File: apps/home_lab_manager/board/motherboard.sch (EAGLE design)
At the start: 18 parts, among them X1 22-23-2021

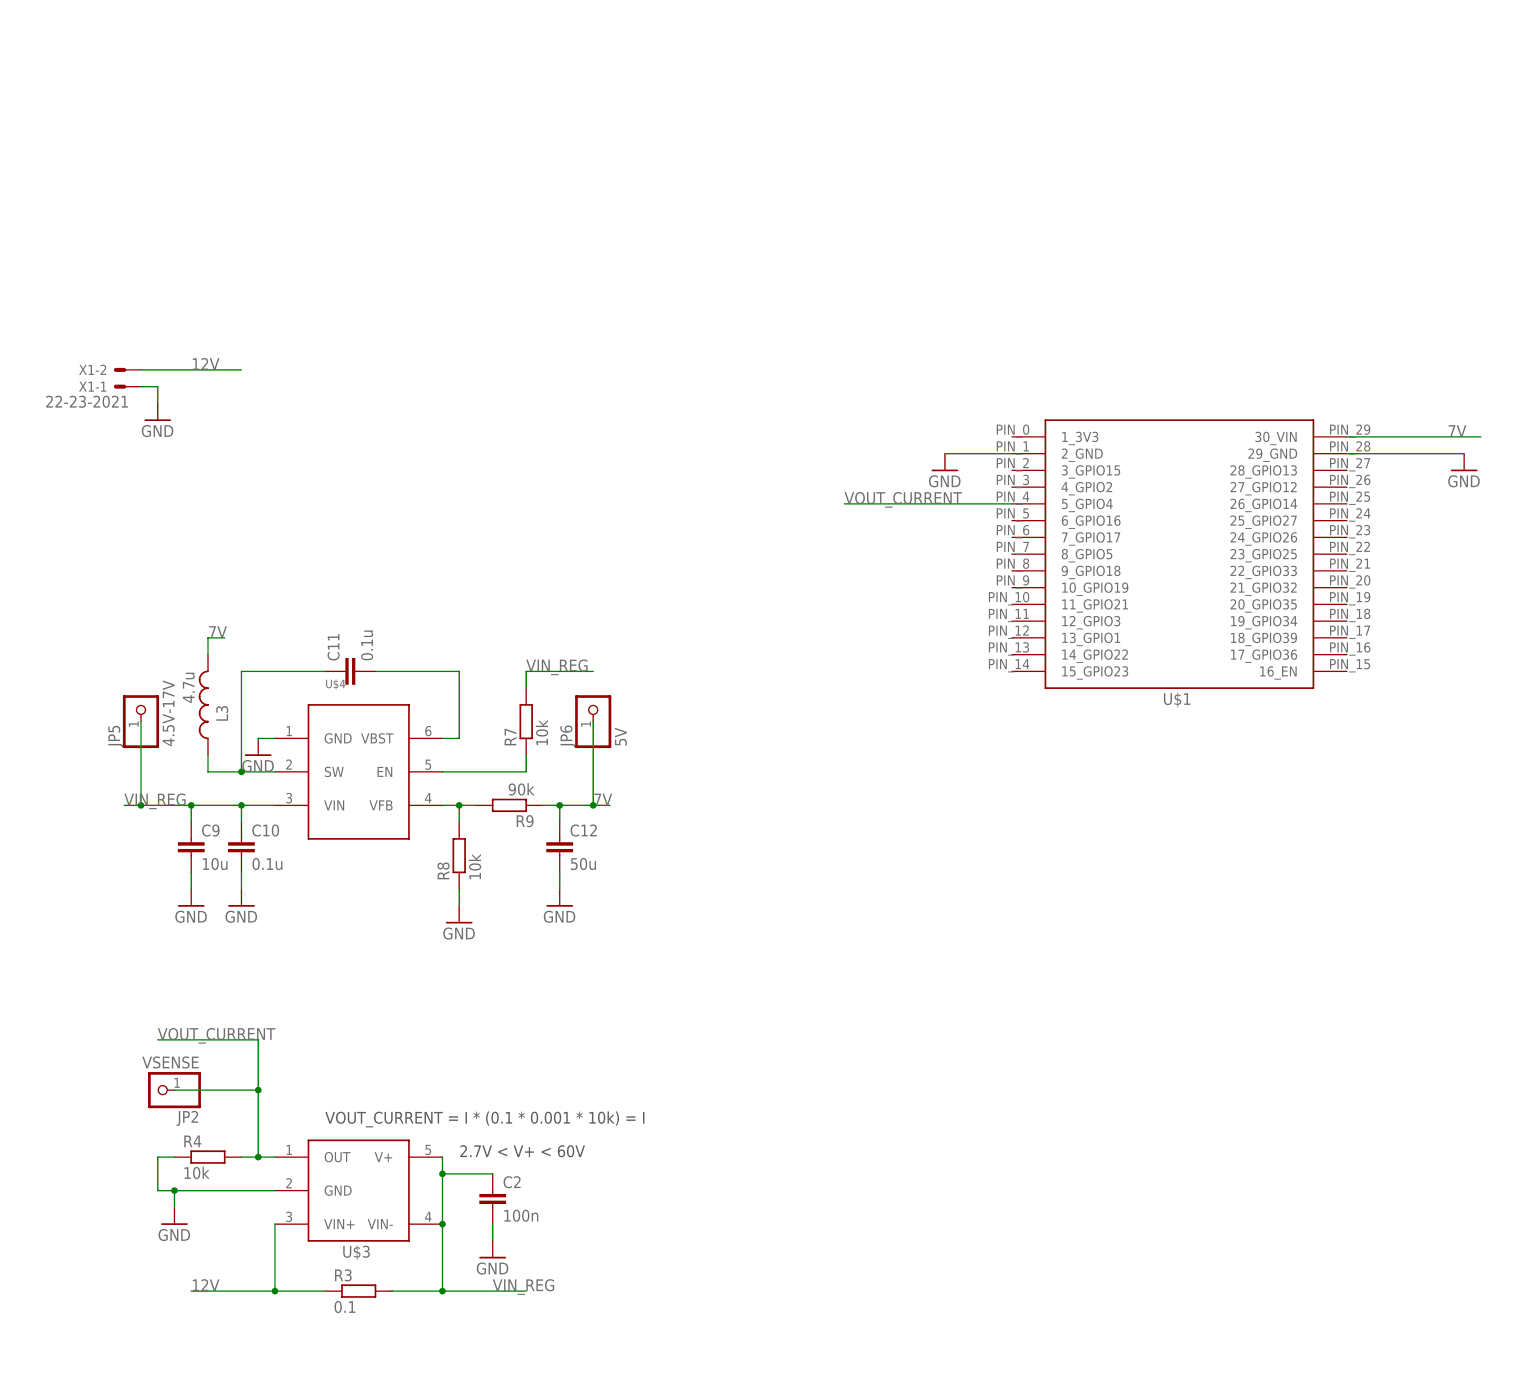
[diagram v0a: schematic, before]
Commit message: Adding mq-2 gaz sensor (wip)
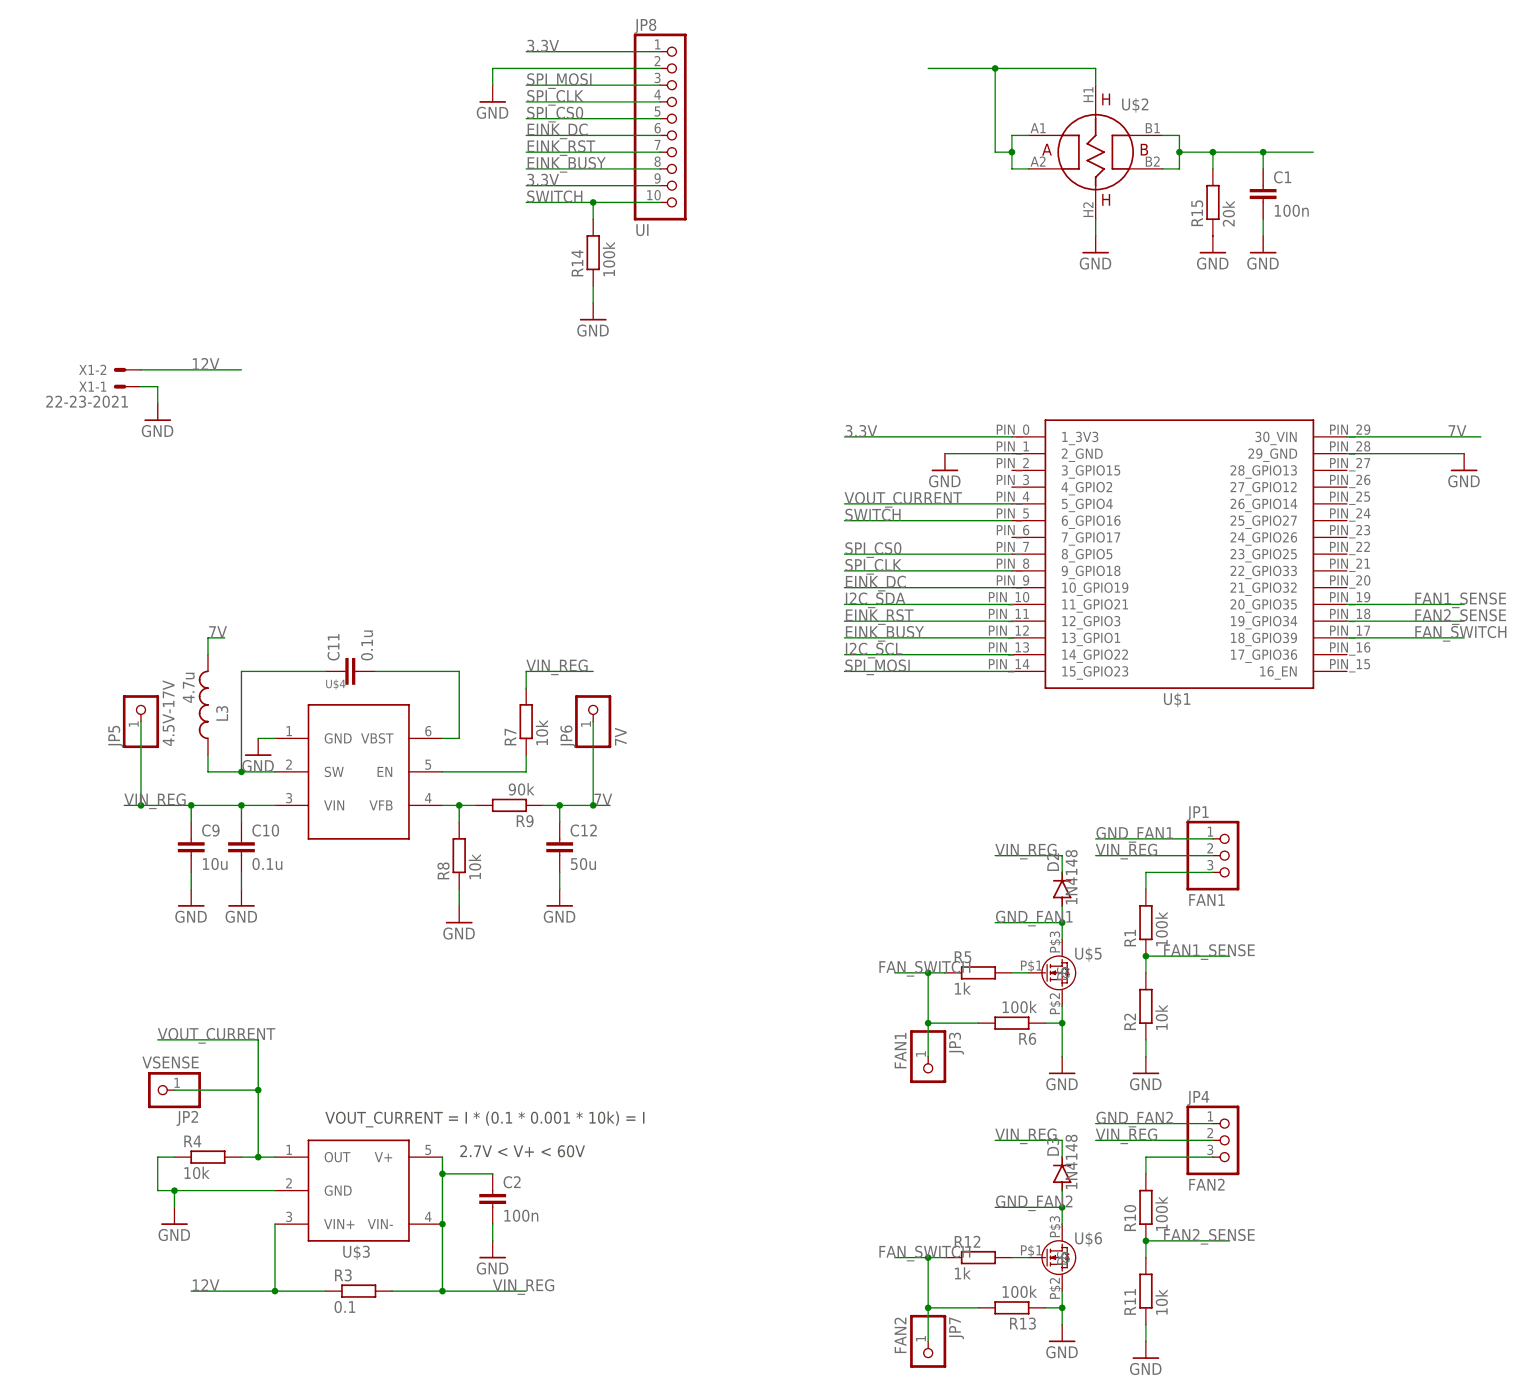
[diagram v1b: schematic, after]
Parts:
- added C1: 100n, rcl:C-EUC0805
- added D2, D3: 1N4148, diode:DIODE-DO-214AC
- added JP1: FAN1, pinhead:PINHD-1X3
- added JP3: FAN1, pinhead:PINHD-1X1
- added JP4: FAN2, pinhead:PINHD-1X3
- added JP7: FAN2, pinhead:PINHD-1X1
- added JP8: UI, pinhead:PINHD-1X10
- added R1, R10, R13, R14, R6: 100k, rcl:R-EU_R0805
- added R11, R2: 10k, rcl:R-EU_R0805
- added R12, R5: 1k, rcl:R-EU_R0805
- added R15: 20k, rcl:R-EU_R0805
- added U$2: MQ_2, bzd:MQ_2
- added U$5, U$6: MGSF1N03L, bzd:MGSF1N03L
- JP6: value 5V -> 7V
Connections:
- new net 3.3V: JP8.1, JP8.9, U$1.1_3V3
- new net EINK_BUSY: JP8.8, U$1.13_GPIO1
- new net EINK_DC: JP8.6, U$1.10_GPIO19
- new net EINK_RST: JP8.7, U$1.12_GPIO3
- new net FAN1_SENSE: R1.1, R2.2, U$1.20_GPIO35
- new net FAN2_SENSE: R10.1, R11.2, U$1.19_GPIO34
- new net FAN_SWITCH: JP3.1, JP7.1, R12.1, R13.2, R5.1, R6.2, U$1.18_GPIO39
- new net GND_FAN1: D2.A, JP1.1, U$5.D
- new net GND_FAN2: D3.A, JP4.1, U$6.D
- new net I2C_SCL: U$1.14_GPIO22
- new net I2C_SDA: U$1.11_GPIO21
- new net N$1: JP1.3, R1.2
- new net N$2: R5.2, U$5.G
- new net N$3: JP4.3, R10.2
- new net N$4: R12.2, U$6.G
- new net N$5: U$2.A1, U$2.A2, U$2.H1
- new net N$6: C1.1, R15.2, U$2.B1, U$2.B2
- new net SPI_CLK: JP8.4, U$1.9_GPIO18
- new net SPI_CS0: JP8.5, U$1.8_GPIO5
- new net SPI_MOSI: JP8.3, U$1.15_GPIO23
- new net SWITCH: JP8.10, R14.2, U$1.6_GPIO16
- net GND: now also C1.2, JP8.2, R11.1, R13.1, R14.1, R15.1, R2.1, R6.1, U$2.H2, U$5.S, U$6.S
- net VIN_REG: now also D2.C, D3.C, JP1.2, JP4.2
